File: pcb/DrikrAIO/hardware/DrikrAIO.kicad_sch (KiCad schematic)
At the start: 0 parts

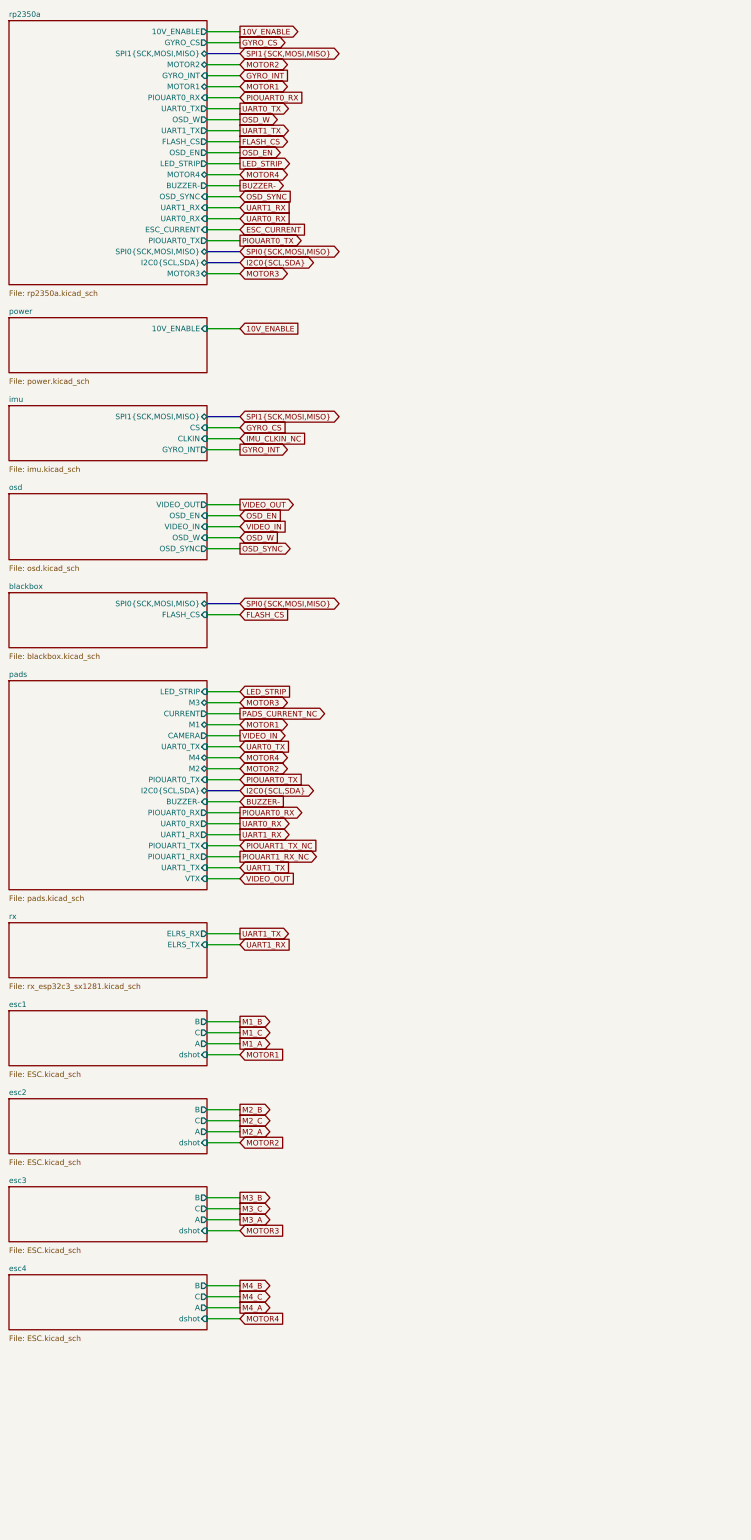
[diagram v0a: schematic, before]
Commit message: DrikrAIO: the power block the sub-sheets came without
The 25 ERC errors were one missing block. OpenESC-30x30 keeps its battery
entry, shunts, current sense and both regulators on its ROOT sheet alongside
the four channel sheets, so copying ESC.kicad_sch brought the power stages
across with nothing to power them.

esc_power.kicad_sch lifts that root, drops only the four channel sheets, and
puts a hierarchical label on each pin they vacated so the existing routing
carries up to our root instead of dangling.

U3 STAYS, AND THAT IS THE POINT. An earlier pass deleted it as "OpenESC's board
outline". It is not an outline -- it is the ESC's entire pad set: VBAT, BATGND,
CUR, M1-M4 and the twelve motor phase pads 1A..4C. Removing it took out the
battery entry and every motor output in one move, and the name is what talked
me into it. Keeping it closed two open items at once.

Verified in the netlist rather than asserted: ESC_CURRENT runs from the INA186
to the FC's ADC divider, +BATT reaches 31 nodes across FC and all four
channels, +10V reaches all four gate-driver decouplers, M1_A runs from the
channel-1 MOSFETs to its pad, and MOTOR1 runs from the FC MCU to the channel-1
DShot input. 347 components, 332 nets.

ERC IS 30 ERRORS AND THAT IS THE FLOOR, NOT A FAILURE. The donors ship with the
same classes -- OpenFC-Lite-Mini, which has flown, reports 8
power_pin_not_driven; OpenESC-30x30, in production, reports 24 pin_not_driven
and 3 power_pin_not_driven. Summed across what we instantiate the donor
baseline is about 37 and this sits below it. PWR_FLAGs were tried on +BATT and
GND and reverted: they cleared none of the old errors and added two new
label_dangling, and by the OpenDrone rule a new error type is a regression
where an existing one is not. FLAGGED_RAILS is left empty with the reasoning
in place so the next person does not repeat it.

Also recorded: +3.3V and +3V3 are DIFFERENT NETS -- the FC rail and the ESC
rail, deliberately separate because the FC's is gated b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
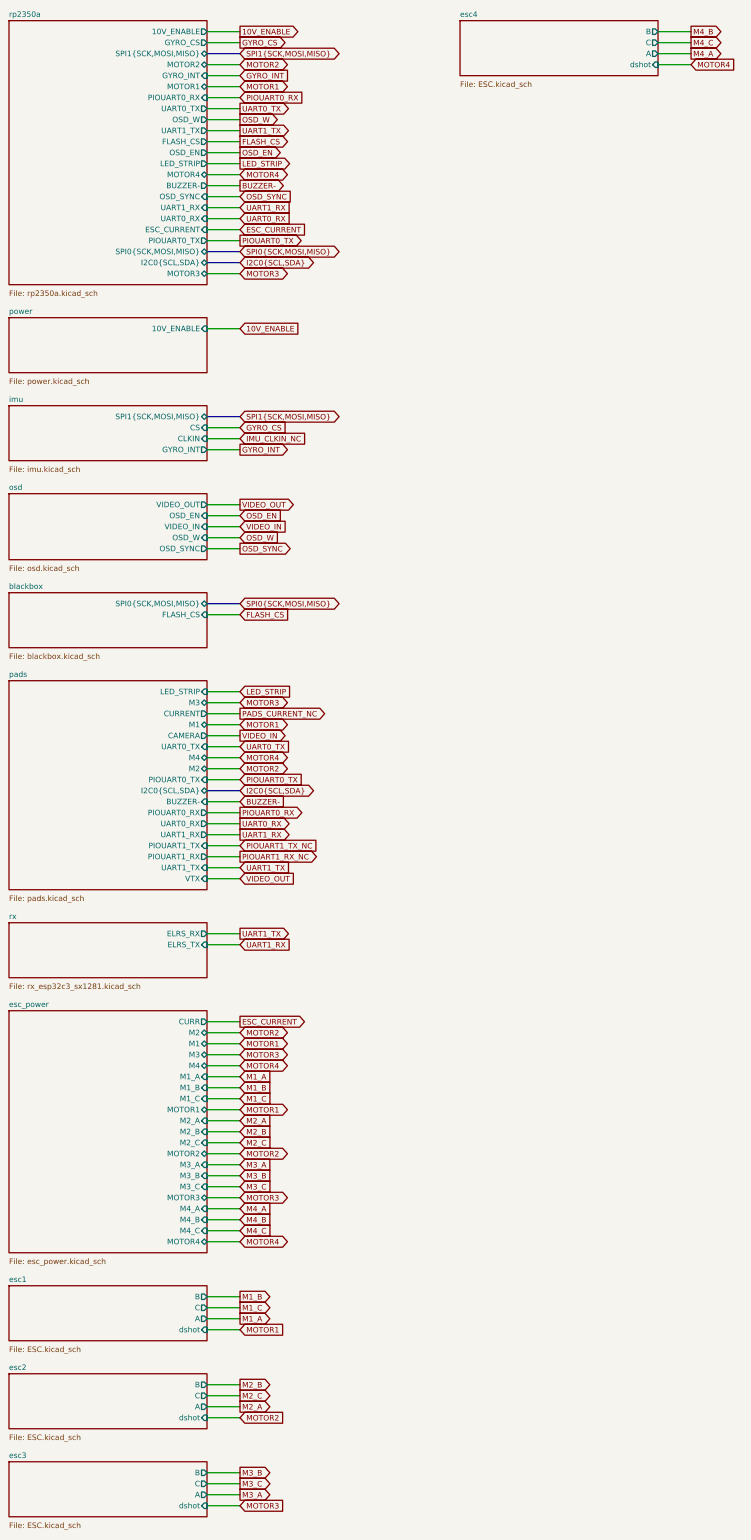
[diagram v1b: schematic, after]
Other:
- added sheet esc_power (esc_power.kicad_sch)
